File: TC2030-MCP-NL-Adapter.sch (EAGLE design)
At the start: 5 parts, among them J1 95501-6669

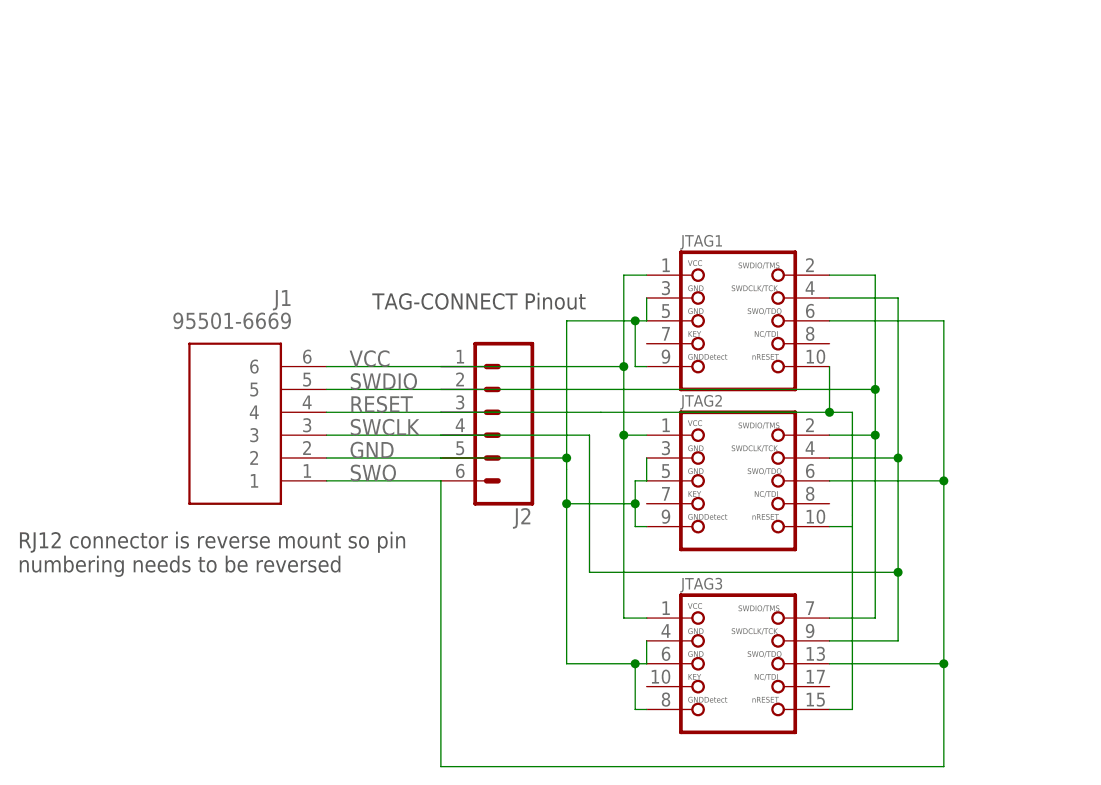
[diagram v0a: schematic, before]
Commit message: update RJ12 variant with 6p connector
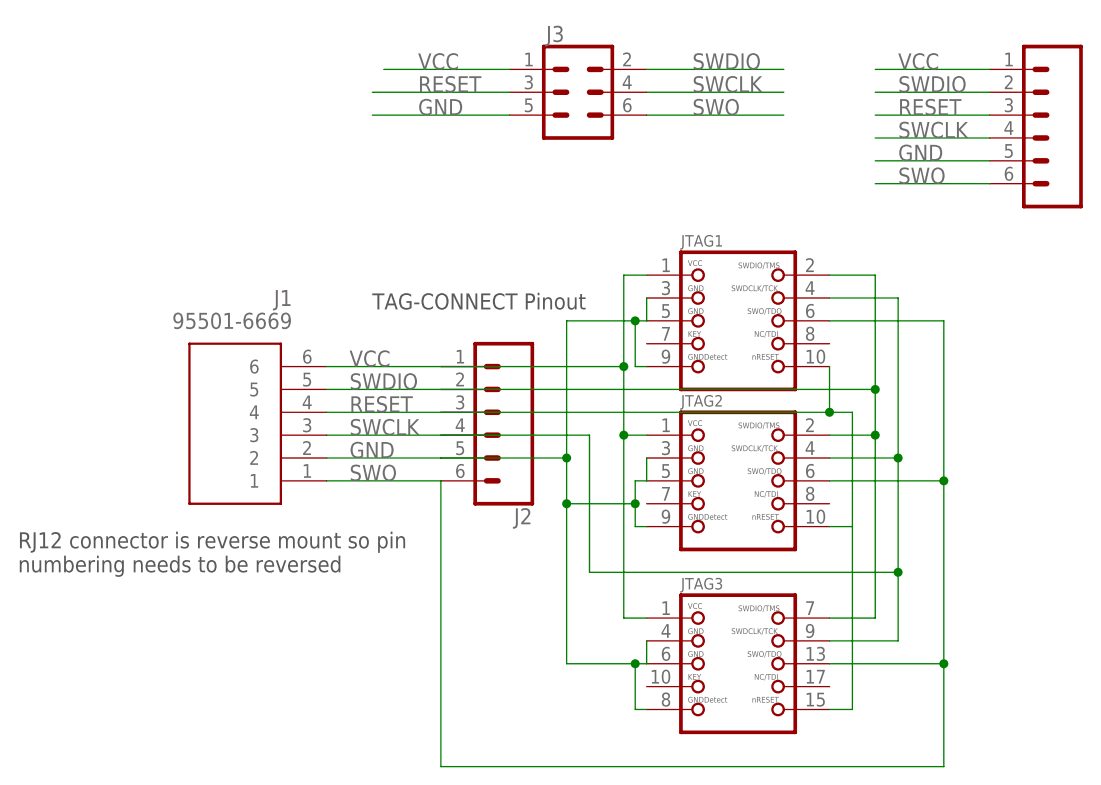
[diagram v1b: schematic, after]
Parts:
- added J3: (no value), SparkFun-Connectors:CONN_03X2NO_SILK
- added J6: (no value), SparkFun-Connectors:CONN_06SILK_FEMALE_PTH
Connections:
- net GND: now also J3.5, J6.5
- net RESET: now also J3.3, J6.3
- net SWCLK: now also J3.4, J6.4
- net SWDIO: now also J3.2, J6.2
- net SWO: now also J3.6, J6.6
- net VCC: now also J3.1, J6.1
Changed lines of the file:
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@@
 <setting verticaltext="up"/>
 </settings>
-<grid distance="0.05" unitdist="inch" unit="inch" style="lines" multiple="1" display="no" altdistance="0.01" altunitdist="inch" altunit="inch"/>
+<grid distance="0.1" unitdist="inch" unit="inch" style="lines" multiple="1" display="no" altdistance="0.01" altunitdist="inch" altunit="inch"/>
 <layers>
 <layer number="1" name="Top" color="4" fill="1" visible="no" active="no"/>
@@
 <part name="JTAG2" library="microbuilder" library_urn="urn:adsk.eagle:library:25095254" deviceset="JTAG-CORTEXM3" device="MOLEX" package3d_urn="urn:adsk.eagle:package:25096189/3"/>
 <part name="JTAG3" library="microbuilder" library_urn="urn:adsk.eagle:library:25095254" deviceset="JTAG-CORTEXM3" device="MOLEX20" package3d_urn="urn:adsk.eagle:package:25096088/1"/>
+<part name="J3" library="SparkFun-Connectors" deviceset="CONN_03X2" device="NO_SILK"/>
+<part name="J6" library="SparkFun-Connectors" deviceset="CONN_06" device="SILK_FEMALE_PTH"/>
 </parts>
 <sheets>
@@
 <attribute name="NAME" x="54.61" y="-4.445" size="1.27" layer="95"/>
 <attribute name="VALUE" x="54.61" y="-22.225" size="1.27" layer="96"/>
+</instance>
+<instance part="J3" gate="G$1" x="43.18" y="50.8" smashed="yes">
+<attribute name="NAME" x="39.624" y="56.388" size="1.778" layer="95" font="vector"/>
+<attribute name="VALUE" x="39.878" y="44.958" size="1.778" layer="96" font="vector" align="top-left"/>
+</instance>
+<instance part="J6" gate="G$1" x="93.98" y="48.26" smashed="yes" rot="R180">
+<attribute name="VALUE" x="99.06" y="58.166" size="1.778" layer="96" font="vector" rot="R180"/>
 </instance>
 </instances>
@@
 <junction x="83.82" y="-12.7"/>
 </segment>
+<segment>
+<wire x1="50.8" y1="48.26" x2="66.04" y2="48.26" width="0.1524" layer="91"/>
+<label x="55.88" y="48.26" size="1.778" layer="95"/>
+<pinref part="J3" gate="G$1" pin="6"/>
+</segment>
+<segment>
+<wire x1="76.2" y1="40.64" x2="88.9" y2="40.64" width="0.1524" layer="91"/>
+<label x="78.74" y="40.64" size="1.778" layer="95"/>
+<pinref part="J6" gate="G$1" pin="6"/>
+</segment>
 </net>
 <net name="GND" class="0">
@@
 <pinref part="J2" gate="G$1" pin="5"/>
 <wire x1="27.94" y1="10.16" x2="41.91" y2="10.16" width="0.1524" layer="91"/>
-<wire x1="41.91" y1="10.16" x2="41.91" y2="8.89" width="0.1524" layer="91"/>
 <pinref part="JTAG2" gate="G$1" pin="5"/>
 <pinref part="JTAG2" gate="G$1" pin="3"/>
@@
 <wire x1="49.53" y1="5.08" x2="49.53" y2="7.62" width="0.1524" layer="91"/>
 <wire x1="49.53" y1="7.62" x2="50.8" y2="7.62" width="0.1524" layer="91"/>
-<wire x1="41.91" y1="8.89" x2="41.91" y2="5.08" width="0.1524" layer="91"/>
+<wire x1="41.91" y1="10.16" x2="41.91" y2="5.08" width="0.1524" layer="91"/>
 <wire x1="41.91" y1="5.08" x2="49.53" y2="5.08" width="0.1524" layer="91"/>
 <pinref part="JTAG1" gate="G$1" pin="5"/>
@@
 <junction x="41.91" y="10.16"/>
 </segment>
+<segment>
+<wire x1="20.32" y1="48.26" x2="35.56" y2="48.26" width="0.1524" layer="91"/>
+<label x="25.4" y="48.26" size="1.778" layer="95"/>
+<pinref part="J3" gate="G$1" pin="5"/>
+</segment>
+<segment>
+<wire x1="76.2" y1="43.18" x2="88.9" y2="43.18" width="0.1524" layer="91"/>
+<label x="78.74" y="43.18" size="1.778" layer="95"/>
+<pinref part="J6" gate="G$1" pin="5"/>
+</segment>
 </net>
 <net name="SWCLK" class="0">
@@
 <junction x="78.74" y="-2.54"/>
 </segment>
+<segment>
+<wire x1="50.8" y1="50.8" x2="66.04" y2="50.8" width="0.1524" layer="91"/>
+<label x="55.88" y="50.8" size="1.778" layer="95"/>
+<pinref part="J3" gate="G$1" pin="4"/>
+</segment>
+<segment>
+<wire x1="76.2" y1="45.72" x2="88.9" y2="45.72" width="0.1524" layer="91"/>
+<label x="78.74" y="45.72" size="1.778" layer="95"/>
+<pinref part="J6" gate="G$1" pin="4"/>
+</segment>
 </net>
 <net name="RESET" class="0">
@@
 <label x="17.78" y="15.24" size="1.778" layer="95"/>
 <pinref part="J2" gate="G$1" pin="3"/>
-<wire x1="27.94" y1="15.24" x2="45.72" y2="15.24" width="0.1524" layer="91"/>
 <pinref part="JTAG1" gate="G$1" pin="10"/>
-<wire x1="45.72" y1="15.24" x2="71.12" y2="15.24" width="0.1524" layer="91"/>
+<wire x1="27.94" y1="15.24" x2="71.12" y2="15.24" width="0.1524" layer="91"/>
 <wire x1="71.12" y1="15.24" x2="71.12" y2="20.32" width="0.1524" layer="91"/>
 <wire x1="71.12" y1="15.24" x2="73.66" y2="15.24" width="0.1524" layer="91"/>
-<wire x1="73.66" y1="15.24" x2="73.66" y2="3.81" width="0.1524" layer="91"/>
+<wire x1="73.66" y1="15.24" x2="73.66" y2="2.54" width="0.1524" layer="91"/>
 <pinref part="JTAG2" gate="G$1" pin="10"/>
-<wire x1="73.66" y1="3.81" x2="73.66" y2="2.54" width="0.1524" layer="91"/>
 <wire x1="73.66" y1="2.54" x2="71.12" y2="2.54" width="0.1524" layer="91"/>
 <pinref part="JTAG3" gate="G$1" pin="10"/>
@@
 <wire x1="73.66" y1="-17.78" x2="71.12" y2="-17.78" width="0.1524" layer="91"/>
 <junction x="71.12" y="15.24"/>
+</segment>
+<segment>
+<wire x1="20.32" y1="50.8" x2="35.56" y2="50.8" width="0.1524" layer="91"/>
+<label x="25.4" y="50.8" size="1.778" layer="95"/>
+<pinref part="J3" gate="G$1" pin="3"/>
+</segment>
+<segment>
+<wire x1="76.2" y1="48.26" x2="88.9" y2="48.26" width="0.1524" layer="91"/>
+<label x="78.74" y="48.26" size="1.778" layer="95"/>
+<pinref part="J6" gate="G$1" pin="3"/>
 </segment>
 </net>
@@
 <junction x="76.2" y="17.78"/>
 </segment>
+<segment>
+<wire x1="50.8" y1="53.34" x2="66.04" y2="53.34" width="0.1524" layer="91"/>
+<label x="55.88" y="53.34" size="1.778" layer="95"/>
+<pinref part="J3" gate="G$1" pin="2"/>
+</segment>
+<segment>
+<wire x1="76.2" y1="50.8" x2="88.9" y2="50.8" width="0.1524" layer="91"/>
+<label x="78.74" y="50.8" size="1.778" layer="95"/>
+<pinref part="J6" gate="G$1" pin="2"/>
+</segment>
 </net>
 <net name="VCC" class="0">
@@
 <junction x="48.26" y="12.7"/>
 </segment>
-</net>
+<segment>
+<wire x1="21.59" y1="53.34" x2="35.56" y2="53.34" width="0.1524" layer="91"/>
+<label x="25.4" y="53.34" size="1.778" layer="95"/>
+<pinref part="J3" gate="G$1" pin="1"/>
+</segment>
+<segment>
+<wire x1="76.2" y1="53.34" x2="88.9" y2="53.34" width="0.1524" layer="91"/>
+<label x="78.74" y="53.34" size="1.778" layer="95"/>
+<pinref part="J6" gate="G$1" pin="1"/>
+</segment>
+</net>
